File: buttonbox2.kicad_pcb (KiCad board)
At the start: 2 copper layers, 125 x 199.9 mm, 172 parts, among them J2 AVR-PDI-6, J3 USB_C_Receptacle_USB2.0, J4 Conn_01x03_Male, J6 Micro_SD_Card, Q1 2N7002, SW10 SW_Push, SW11 SW_Push, SW12 SW_Push, SW13 SW_Push, SW14 SW_Push, SW15 SW_Push, SW16 SW_Push, SW17 SW_Push, SW18 SW_Push, SW19 SW_Push, SW20 SW_Push, SW21 SW_Push, SW22 SW_Push, SW23 SW_Push, SW24 SW_Push, SW25 SW_Push, SW26 SW_Push, SW27 SW_Push, SW28 SW_Push, SW29 SW_Push, SW30 SW_Push, SW31 SW_Push, SW32 SW_Push, SW33 SW_Push, SW34 SW_Push, SW35 SW_Push, SW36 SW_Push, SW37 SW_Push, SW38 SW_Push, SW39 SW_Push, SW40 SW_Push, SW5 SW_Push, SW6 SW_Push, SW7 SW_Push, SW8 SW_Push, SW9 SW_Push, U1 ATxmega256A3-AU, U10 MC34063AD, U11 PT6311, U12 VFD_HNV-12SS62, U2 LM4871, U3 YX5200-24SS, U4 SY6926, U5 DMG3415, U6 AMS1117-3.3, U7 DMG3415, U8 LM4871, Y2 Crystal_GND24

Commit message: Ja crap toch weer aan de PCB gezeten
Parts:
- removed H1, H2, H3: MountingHole, MountingHole:MountingHole_3.2mm_M3
- added SW1: SW_SP3T, Hardware:schakelaar, F.Cu at (198.1, -18.2)
- added SW2: SW_SPDT, Hardware:SWINTCHFORBATTERY, F.Cu at (76.6, -8.90)
- moved C11 57.0 mm to (46.2, -13.5)
- moved C13 57.0 mm to (29.1, -3.74)
- moved C14 57.0 mm to (26.8, -19.1)
- moved C17 57.0 mm to (33.6, -4.09)
- moved C18 57.0 mm to (54.6, -28.4)
- moved C28 57.0 mm to (46.2, -27.9)
- moved C29 57.0 mm to (13.4, -12.0)
- moved C31 57.0 mm to (43.3, -16.5)
- moved C32 57.0 mm to (26.8, -27.2)
- moved C34 57.0 mm to (-19.6, -19.3)
- moved C35 57.0 mm to (-10.5, -31.5)
- moved D10 57.0 mm to (13.3, -50.9)
- moved D5 57.0 mm to (40.6, -9.82)
- moved D8 57.0 mm to (-14.9, -25.5)
- moved R10 57.0 mm to (43.7, -6.83)
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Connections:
- BT2 pad 1: BAT -> Net-(BT2-Pad1)
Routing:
- net Row6: track 198.6 -> 0.00 mm, vias 10 -> 0
- net Row5: track 188.9 -> 0.00 mm, vias 8 -> 0
- net Row4: track 155.8 -> 0.00 mm, vias 6 -> 0
- net Column1: track 138.3 -> 0.00 mm
- net Row3: track 135.7 -> 0.00 mm, vias 4 -> 0
- net Column2: track 134.3 -> 0.00 mm
- net Row2: track 119.8 -> 0.00 mm, vias 2 -> 0
- net Column4: track 115.3 -> 0.00 mm
- net Column6: track 113.4 -> 0.00 mm
- net Column3: track 101.8 -> 0.00 mm
- net Column5: track 97.3 -> 0.00 mm
- net Row1: track 96.3 -> 0.00 mm
- net +3V3: track 88.4 -> 0.00 mm, vias 2 -> 0
- net /MP3_player/3V3OUT: track 67.8 -> 0.00 mm, vias 4 -> 0
- net PLAYER_ON: track 46.2 -> 0.00 mm, vias 2 -> 0
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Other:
- board size 125 x 199.9 mm -> 125 x 209.8 mm

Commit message: Added SY6926 component values and some minor cleanup
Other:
- board text removed: "ROMEINSE HOMO SEKS"

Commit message: Slight footprint shuffle for the VFD
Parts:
- BT2, C1, C10, C12, C15, C16, C19, C2, C20, C21, C22, C23, C24, C25, C26, C3, C4, C7, C8, C9, Cams1, Cbs1, Cbus1, Csin1, Csnubber1, Csys1, Ctim1, D1, J2, J3, J4, J6, Q1, R1, R11, R12, R13, R14, R15, R18, R2, R20, R21, R3, R4, R5, R6, Rnor1, Rntc1, Rsnubber1, U1, U2, U3, U4, U5, U6, U7, U8, Y2: moved to F.Cu
- C14, C18, C27, C28, C29, C32, L2, R16, R22, R23, RV1, RV2, SW1, U10, U11: moved to B.Cu
- C5, C6: value 22p -> 10p; moved to F.Cu
- Cin1: value C -> 20uF; moved to F.Cu
- L1: value L -> 1.65uH; moved to F.Cu
- LSL1: renamed from LS1; moved to F.Cu
- LSR1: renamed from LS2; moved to F.Cu
- Rdm1, Rfb1: value R -> 33K; moved to F.Cu
- Rdm2: value R -> 9.1K; moved to F.Cu
- Ricgh1: value R -> 10.666K; moved to F.Cu
- Rin1: value R -> 1K; moved to F.Cu
- Risys1: value R -> 36K; moved to F.Cu
- fb2: value R -> 10.3K; moved to F.Cu
- moved C35 195.2 mm to (173.2, -97.5)
- moved D8 195.2 mm to (168.8, -91.5)
- moved R30 195.2 mm to (164.1, -82.3)
- moved R34 195.2 mm to (168.8, -88.5)
- moved R41 195.2 mm to (173.2, -88.5)
- moved R45 195.2 mm to (168.5, -82.3)
- moved R46 195.2 mm to (164.1, -79.4)
- moved C33 195.2 mm to (168.8, -97.5)
- moved C34 195.2 mm to (164.1, -85.3)
- moved C36 195.2 mm to (168.8, -94.5)
- moved D7 195.2 mm to (159.5, -74.1)
- moved D9 195.2 mm to (173.3, -94.5)
- moved R43 195.2 mm to (163.9, -74.2)
- moved TP1 195.2 mm to (172.8, -82.1)
- moved D10 182.5 mm to (185.5, -111.1)
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
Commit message: alles op B.cu ivm assemblage
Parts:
- BT2, C1, C10, C12, C15, C16, C19, C2, C20, C21, C22, C23, C24, C25, C26, C3, C4, C5, C6, C7, C8, C9, Cams1, Cbs1, Cbus1, Cin1, Csin1, Csnubber1, Csys1, Ctim1, D1, J2, J3, J4, J6, L1, LSL1, LSR1, Q1, R1, R11, R12, R13, R14, R15, R18, R2, R20, R21, R29, R3, R4, R5, R6, Rdm1, Rdm2, Rfb1, Ricgh1, Rin1, Risys1, Rnor1, Rntc1, Rsnubber1, SW2, U1, U2, U3, U4, U5, U6, U7, U8, Y2, fb2: moved to B.Cu
- SW1: moved to F.Cu
- moved SW2 121.4 mm to (75.8, -12.8)
- moved SW1 121.0 mm to (197.0, 7.00)
- moved J3 119.0 mm to (77.0, 4.00)
- moved U6 114.5 mm to (79.2, 20.9), turned to 0 degrees
- moved R29 112.2 mm to (80.4, 37.6)
- moved J6 112.1 mm to (192.5, 31.2)
- moved Cams1 107.0 mm to (83.0, 14.1)
- moved Rin1 106.4 mm to (83.3, 11.1), turned to 180 degrees
- moved C10 101.0 mm to (86.0, 29.2)
- moved Rdm2 97.6 mm to (87.7, 14.0), turned to 180 degrees
- moved Rntc1 97.6 mm to (87.7, 11.1), turned to 180 degrees
- moved Risys1 97.5 mm to (87.8, 17.1), turned to 180 degrees
- moved C7 95.9 mm to (184.4, 17.9)
- moved R2 95.9 mm to (184.4, 13.9)
- moved R3 95.9 mm to (184.4, 9.91)
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
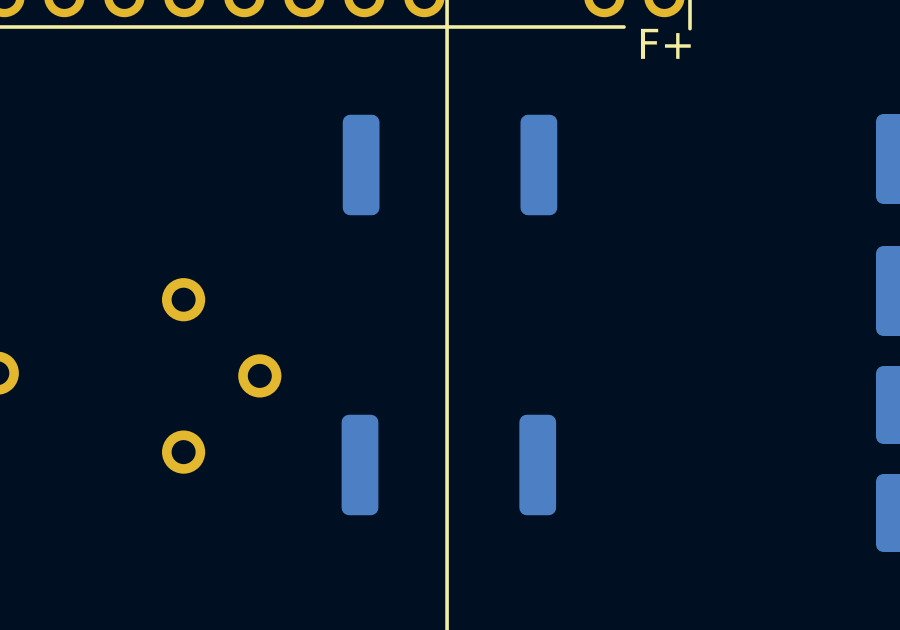
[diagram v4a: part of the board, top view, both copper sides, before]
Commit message: Added footprint of U9
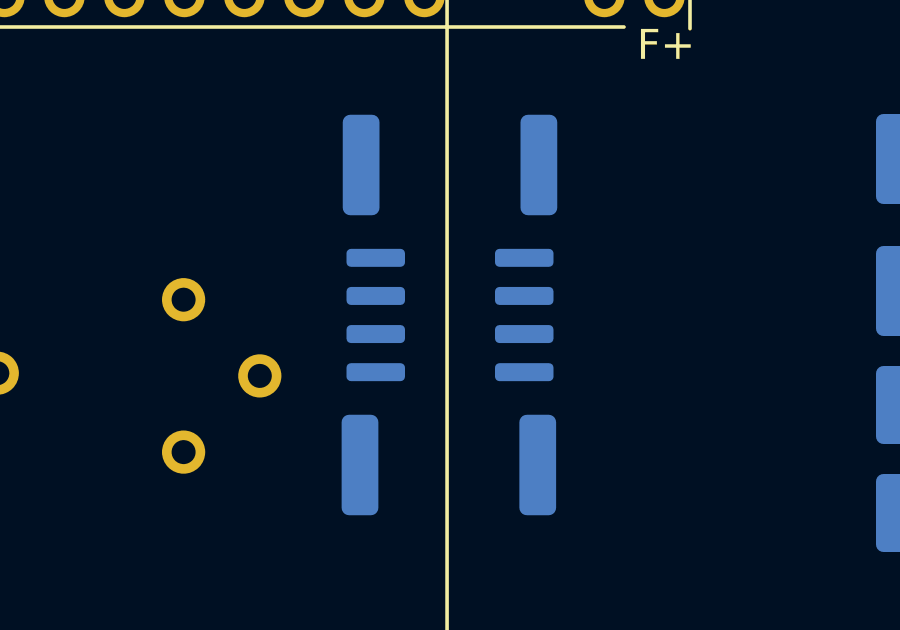
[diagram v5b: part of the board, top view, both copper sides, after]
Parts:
- added U9: LM4871, Package_SO:SOIC-8_3.9x4.9mm_P1.27mm, B.Cu at (166.0, -18.0)
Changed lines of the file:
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@@
     (tracks 0)
     (zones 0)
-    (modules 171)
+    (modules 172)
     (nets 195)
   )
@@
     (add_net VIN)
   )
+  (module Package_SO:SOIC-8_3.9x4.9mm_P1.27mm (layer B.Cu)
+    (at 166 -18)
+    (descr "SOIC, 8 Pin (JEDEC MS-012AA, https://www.analog.com/media/en/package-pcb-resources/package/pkg_pdf/soic_narrow-r/r_8.pdf), generated with kicad-footprint-generator ipc_gullwing_generator.py")
+    (tags "SOIC SO")
+    (attr smd)
+    (fp_text reference U9 (at 0 3.4) (layer B.SilkS)
+      (effects (font (size 1 1) (thickness 0.15)) (justify mirror))
+    )
+    (fp_text value LM4871 (at 0 -3.4) (layer B.Fab)
+      (effects (font (size 1 1) (thickness 0.15)) (justify mirror))
+    )
+    (fp_text user %R (at 0 0) (layer B.Fab)
+      (effects (font (size 0.98 0.98) (thickness 0.15)) (justify mirror))
+    )
+    (fp_line (start 0 -2.56) (end 1.95 -2.56) (layer B.SilkS) (width 0.12))
+    (fp_line (start 0 -2.56) (end -1.95 -2.56) (layer B.SilkS) (width 0.12))
+    (fp_line (start 0 2.56) (end 1.95 2.56) (layer B.SilkS) (width 0.12))
+    (fp_line (start 0 2.56) (end -3.45 2.56) (layer B.SilkS) (width 0.12))
+    (fp_line (start -0.975 2.45) (end 1.95 2.45) (layer B.Fab) (width 0.1))
+    (fp_line (start 1.95 2.45) (end 1.95 -2.45) (layer B.Fab) (width 0.1))
+    (fp_line (start 1.95 -2.45) (end -1.95 -2.45) (layer B.Fab) (width 0.1))
+    (fp_line (start -1.95 -2.45) (end -1.95 1.475) (layer B.Fab) (width 0.1))
+    (fp_line (start -1.95 1.475) (end -0.975 2.45) (layer B.Fab) (width 0.1))
+    (fp_line (start -3.7 2.7) (end -3.7 -2.7) (layer B.CrtYd) (width 0.05))
+    (fp_line (start -3.7 -2.7) (end 3.7 -2.7) (layer B.CrtYd) (width 0.05))
+    (fp_line (start 3.7 -2.7) (end 3.7 2.7) (layer B.CrtYd) (width 0.05))
+    (fp_line (start 3.7 2.7) (end -3.7 2.7) (layer B.CrtYd) (width 0.05))
+    (pad 8 smd roundrect (at 2.475 1.905) (size 1.95 0.6) (layers B.Cu B.Paste B.Mask) (roundrect_rratio 0.25)
+      (net 134 "Net-(R23-Pad2)"))
+    (pad 7 smd roundrect (at 2.475 0.635) (size 1.95 0.6) (layers B.Cu B.Paste B.Mask) (roundrect_rratio 0.25)
+      (net 103 PGNDBAT))
+    (pad 6 smd roundrect (at 2.475 -0.635) (size 1.95 0.6) (layers B.Cu B.Paste B.Mask) (roundrect_rratio 0.25)
+      (net 95 SYS))
+    (pad 5 smd roundrect (at 2.475 -1.905) (size 1.95 0.6) (layers B.Cu B.Paste B.Mask) (roundrect_rratio 0.25)
+      (net 131 "Net-(R10-Pad1)"))
+    (pad 4 smd roundrect (at -2.475 -1.905) (size 1.95 0.6) (layers B.Cu B.Paste B.Mask) (roundrect_rratio 0.25)
+      (net 104 "Net-(C13-Pad1)"))
+    (pad 3 smd roundrect (at -2.475 -0.635) (size 1.95 0.6) (layers B.Cu B.Paste B.Mask) (roundrect_rratio 0.25)
+      (net 130 "Net-(R10-Pad2)"))
+    (pad 2 smd roundrect (at -2.475 0.635) (size 1.95 0.6) (layers B.Cu B.Paste B.Mask) (roundrect_rratio 0.25)
+      (net 107 "Net-(C18-Pad1)"))
+    (pad 1 smd roundrect (at -2.475 1.905) (size 1.95 0.6) (layers B.Cu B.Paste B.Mask) (roundrect_rratio 0.25)
+      (net 103 PGNDBAT))
+    (model ${KISYS3DMOD}/Package_SO.3dshapes/SOIC-8_3.9x4.9mm_P1.27mm.wrl
+      (at (xyz 0 0 0))
+      (scale (xyz 1 1 1))
+      (rotate (xyz 0 0 0))
+    )
+  )
   (module Hardware:SWINTCHFORBATTERY (layer B.Cu)

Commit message: shuffled things around
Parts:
- removed R40, R41, R42, R43, R44, R45, R46, R47: 10K, Resistor_SMD:R_0805_2012Metric
- moved SW1 13.0 mm to (197.0, 20.0)

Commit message: Added a rotary encoder and almost all BC values
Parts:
- removed Rntc1: R, Resistor_SMD:R_0805_2012Metric
- added Cbat1: 20uF, Capacitor_SMD:C_0805_2012Metric, B.Cu at (93.2, 0.59)
- added R36: 10K, Resistor_SMD:R_0805_2012Metric, B.Cu at (83.1, -42.8)
- added R37: 10K, Resistor_SMD:R_0805_2012Metric, B.Cu at (88.2, -42.8)
- added R38: 10K, Resistor_SMD:R_0805_2012Metric, B.Cu at (83.2, -35.2)
- added SW3: Rotary_Encoder_Switch, Rotary_Encoder:RotaryEncoder_Alps_EC11E-Switch_Vertical_H20mm_CircularMountingHoles, F.Cu at (88.2, -46.6)
- Cbus1, Csys1: value C -> 20uF
- Csin1, Ctim1: value C -> 100nF
- Csnubber1: value C -> DNP
- L1: value 1.65uH -> 2.2uH
- Rnor1: value R -> 22K
- Rsnubber1: value R -> DNP
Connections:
- net NTC renamed Net-(R35-Pad1)

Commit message: Final schematic edits, PCB layout
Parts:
- removed SW40: SW_Push, Hardware:SW_Cherry_MX_1.00u_PCB_BETTER
- added D11: D_Small, Diode_SMD:D_SOD-123, B.Cu at (87.0, 47.0)
- added D12: D_Small, Diode_SMD:D_SOD-123, B.Cu at (87.3, 66.0)
- added D13: D_Small, Diode_SMD:D_SOD-123, B.Cu at (87.3, 85.0)
- added D14: D_Small, Diode_SMD:D_SOD-123, B.Cu at (87.0, 104.0)
- added D15: D_Small, Diode_SMD:D_SOD-123, B.Cu at (87.3, 123.0)
- added D16: D_Small, Diode_SMD:D_SOD-123, B.Cu at (87.0, 142.0)
- added D17: D_Small, Diode_SMD:D_SOD-123, B.Cu at (106.3, 47.0)
- added D18: D_Small, Diode_SMD:D_SOD-123, B.Cu at (106.0, 66.0)
- added D19: D_Small, Diode_SMD:D_SOD-123, B.Cu at (106.3, 85.0)
- added D20: D_Small, Diode_SMD:D_SOD-123, B.Cu at (106.0, 104.0)
- added D21: D_Small, Diode_SMD:D_SOD-123, B.Cu at (106.0, 123.0)
- added D22: D_Small, Diode_SMD:D_SOD-123, B.Cu at (106.0, 142.0)
- added D23: D_Small, Diode_SMD:D_SOD-123, B.Cu at (125.3, 47.0)
- added D24: D_Small, Diode_SMD:D_SOD-123, B.Cu at (125.0, 66.0)
- added D25: D_Small, Diode_SMD:D_SOD-123, B.Cu at (125.0, 85.0)
- added D26: D_Small, Diode_SMD:D_SOD-123, B.Cu at (125.0, 104.0)
- added D27: D_Small, Diode_SMD:D_SOD-123, B.Cu at (125.3, 123.0)
- added D28: D_Small, Diode_SMD:D_SOD-123, B.Cu at (125.0, 142.0)
- added D29: D_Small, Diode_SMD:D_SOD-123, B.Cu at (144.0, 47.0)
- added D30: D_Small, Diode_SMD:D_SOD-123, B.Cu at (144.0, 66.0)
- added D31: D_Small, Diode_SMD:D_SOD-123, B.Cu at (144.0, 85.0)
- added D32: D_Small, Diode_SMD:D_SOD-123, B.Cu at (144.0, 104.0)
- added D33: D_Small, Diode_SMD:D_SOD-123, B.Cu at (144.0, 123.0)
- added D34: D_Small, Diode_SMD:D_SOD-123, B.Cu at (144.0, 142.0)
- added D35: D_Small, Diode_SMD:D_SOD-123, B.Cu at (163.0, 47.0)
- added D36: D_Small, Diode_SMD:D_SOD-123, B.Cu at (163.0, 66.0)
- added D37: D_Small, Diode_SMD:D_SOD-123, B.Cu at (163.0, 85.0)
- added D38: D_Small, Diode_SMD:D_SOD-123, B.Cu at (162.7, 104.0)
- added D39: D_Small, Diode_SMD:D_SOD-123, B.Cu at (163.0, 123.0)
- added D40: D_Small, Diode_SMD:D_SOD-123, B.Cu at (163.0, 142.0)
- added D41: D_Small, Diode_SMD:D_SOD-123, B.Cu at (182.0, 47.0)
- added D42: D_Small, Diode_SMD:D_SOD-123, B.Cu at (182.0, 66.0)
- added D43: D_Small, Diode_SMD:D_SOD-123, B.Cu at (182.0, 85.0)
- added D44: D_Small, Diode_SMD:D_SOD-123, B.Cu at (182.0, 104.0)
- added D45: D_Small, Diode_SMD:D_SOD-123, B.Cu at (182.3, 123.0)
- added D46: D_Small, Diode_SMD:D_SOD-123, B.Cu at (182.0, 142.0)
- added R35: 4.4K, Resistor_SMD:R_0805_2012Metric, F.Cu at (98.0, 4.41)
- added SW4: SW_Push, Hardware:SW_Cherry_MX_1.00u_PCB_BETTER, F.Cu at (91.5, 47.9)
- BT2, Cams1, Cbat1, Cbus1, Cin1, Csin1, Csnubber1, Csys1, Ctim1, Rdm1, Rdm2, Rfb1, Ricgh1, Rin1, Risys1, Rnor1, Rsnubber1, U4, U6, fb2: moved to F.Cu
- C11, C13, C17, C30, C31, C33, C34, C35, C36, D10, D2, D3, D4, D5, D7, D8, D9, R10, R17, R19, R24, R25, R26, R27, R30, R31, R32, R33, R34, R39, R7, R8, R9: moved to B.Cu
- Cbs1: value C -> 1nF; moved to F.Cu
- L1: footprint Connector_PinHeader_2.54mm:PinHeader_1x02_P2.54mm_Vertical -> Inductor_SMD:L_Sunlord_MWSA0518_5.4x5.2mm; moved to F.Cu
- moved D10 120.4 mm to (107.9, -19.0)
- moved R31 120.0 mm to (100.9, -15.0), turned to 180 degrees
- moved R29 116.4 mm to (193.8, 11.2), turned to 270 degrees
- moved D6 115.6 mm to (116.0, 16.0)
- moved R28 112.6 mm to (112.0, 16.0)
- moved R34 106.4 mm to (90.9, -16.0), turned to 180 degrees
- moved C35 102.4 mm to (134.0, -3.00)
- moved D9 101.4 mm to (107.9, -17.0)
- moved C36 99.4 mm to (130.1, -3.00)
- moved D8 99.3 mm to (107.9, -13.0)
- moved SW10 96.1 mm to (110.5, 47.9)
- moved SW16 96.1 mm to (129.5, 47.9)
- moved SW22 96.0 mm to (148.5, 47.9)
- moved SW28 96.0 mm to (167.5, 47.9)
- moved SW34 95.9 mm to (186.5, 47.9)
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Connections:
- SW10 pad 1: Row6 -> Net-(D17-Pad2)
- SW10 pad 2: Column1 -> Column2
- SW11 pad 1: Row1 -> Net-(D18-Pad2)
- SW12 pad 1: Row2 -> Net-(D19-Pad2)
- SW13 pad 1: Row3 -> Net-(D20-Pad2)
- SW14 pad 1: Row4 -> Net-(D21-Pad2)
- SW15 pad 1: Row5 -> Net-(D22-Pad2)
- SW16 pad 1: Row6 -> Net-(D23-Pad2)
- SW16 pad 2: Column2 -> Column3
- SW17 pad 1: Row1 -> Net-(D24-Pad2)
- SW18 pad 1: Row2 -> Net-(D25-Pad2)
- SW19 pad 1: Row3 -> Net-(D26-Pad2)
- SW20 pad 1: Row4 -> Net-(D27-Pad2)
- SW21 pad 1: Row5 -> Net-(D28-Pad2)
- SW22 pad 1: Row6 -> Net-(D29-Pad2)
- SW22 pad 2: Column3 -> Column4
- SW23 pad 1: Row1 -> Net-(D30-Pad2)
- SW24 pad 1: Row2 -> Net-(D31-Pad2)
- SW25 pad 1: Row3 -> Net-(D32-Pad2)
- SW26 pad 1: Row4 -> Net-(D33-Pad2)
- SW27 pad 1: Row5 -> Net-(D34-Pad2)
- SW28 pad 1: Row6 -> Net-(D35-Pad2)
- SW28 pad 2: Column4 -> Column5
- SW29 pad 1: Row1 -> Net-(D36-Pad2)
- SW30 pad 1: Row2 -> Net-(D37-Pad2)
- SW31 pad 1: Row3 -> Net-(D38-Pad2)
- SW32 pad 1: Row4 -> Net-(D39-Pad2)
- SW33 pad 1: Row5 -> Net-(D40-Pad2)
- SW34 pad 1: Row6 -> Net-(D41-Pad2)
- SW34 pad 2: Column5 -> Column6
- SW35 pad 1: Row1 -> Net-(D42-Pad2)
- SW36 pad 1: Row2 -> Net-(D43-Pad2)
- SW37 pad 1: Row3 -> Net-(D44-Pad2)
- SW38 pad 1: Row4 -> Net-(D45-Pad2)
- SW39 pad 1: Row5 -> Net-(D46-Pad2)
- SW5 pad 1: Row1 -> Net-(D12-Pad2)
- SW6 pad 1: Row2 -> Net-(D13-Pad2)
- SW7 pad 1: Row3 -> Net-(D14-Pad2)
- SW8 pad 1: Row4 -> Net-(D15-Pad2)
- SW9 pad 1: Row5 -> Net-(D16-Pad2)
- U1 pad 18: Net-(U1-Pad18) -> RX
- U1 pad 19: Net-(U1-Pad19) -> TX
- U1 pad 20: Net-(U1-Pad20) -> LED
- U1 pad 26: HW_RX -> Net-(U1-Pad26)
- U1 pad 27: HW_TX -> Net-(U1-Pad27)
- U1 pad 28: Net-(U1-Pad28) -> HW_RX
- U1 pad 29: Net-(U1-Pad29) -> HW_TX
- U1 pad 6: RX -> Net-(U1-Pad6)
- U1 pad 7: TX -> Net-(U1-Pad7)
- U1 pad 8: LED -> Net-(U1-Pad8)
